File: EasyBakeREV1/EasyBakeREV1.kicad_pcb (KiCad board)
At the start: 2 copper layers, 100 x 71.2 mm, 105 parts, among them J1 I2C OUT, U1 MIC5219-3.3YM5, U2 USBLC6-2SC6, U3 PCA9702, U4 SQ2310ES_SOT23, U5 NHD-C12832A1Z, U6 SQ2310ES_SOT23, U7 MAX31855_SO8, U8 LM324, U9 SN74LVC1G32, Y1 16MHz

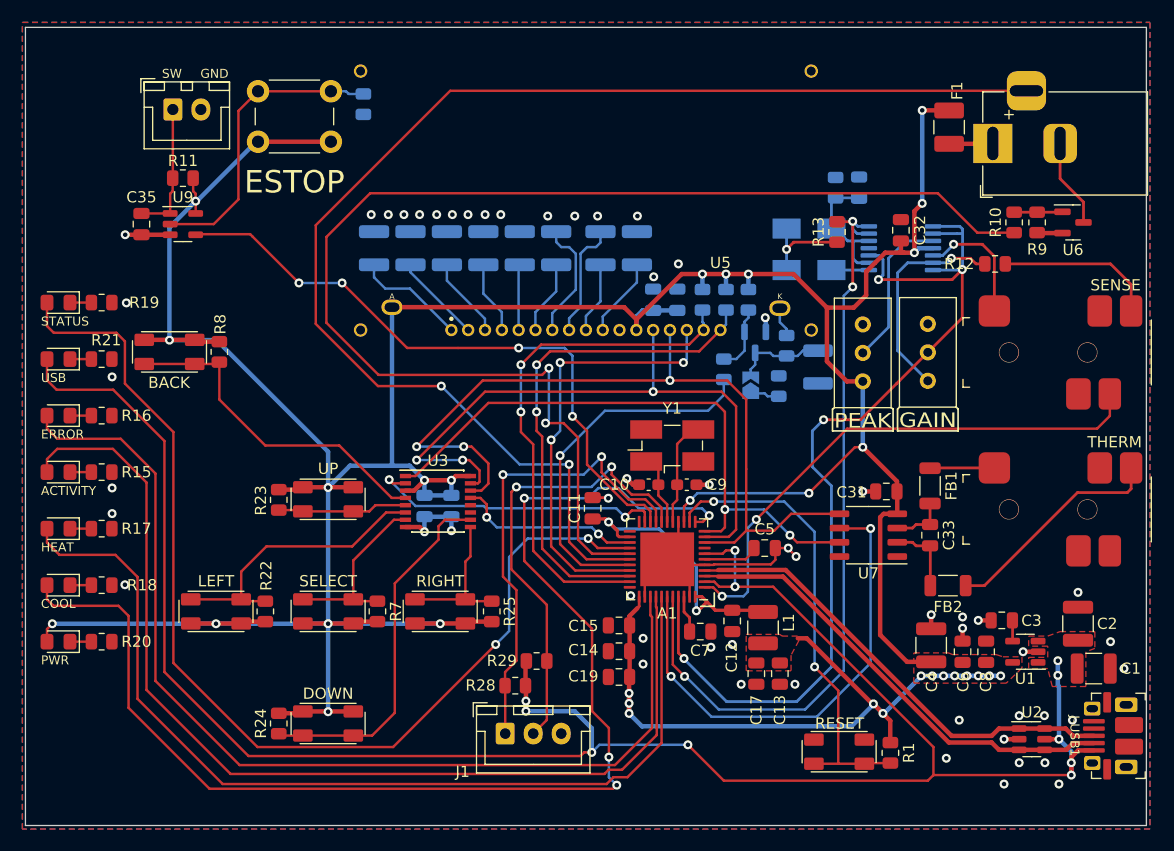
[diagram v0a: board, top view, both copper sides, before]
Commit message: REV3 - Reorganize MC pinouts and add LED driver (WIP)
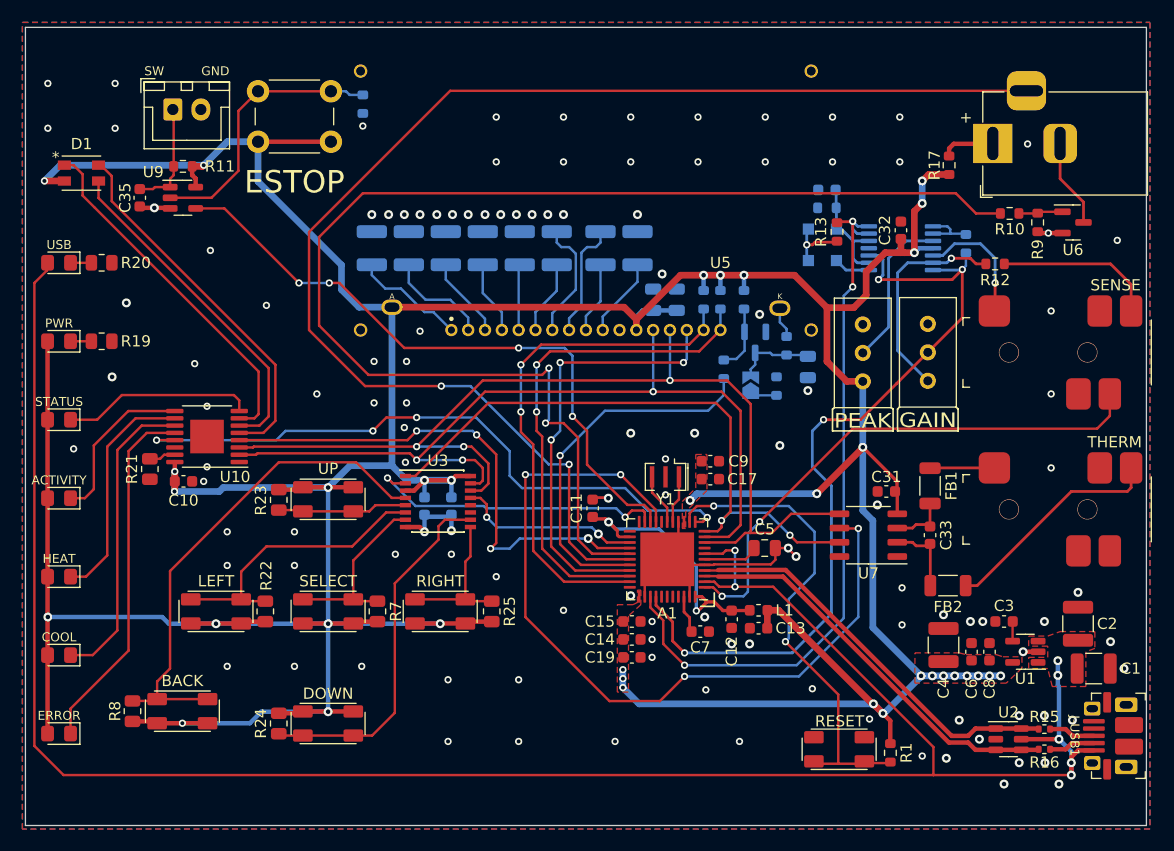
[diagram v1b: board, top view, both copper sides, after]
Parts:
- removed F1: Polyfuse_Small, Fuse:Fuse_1210_3225Metric_Pad1.42x2.65mm_HandSolder
- removed J1: I2C OUT, Connector_JST:JST_XH_B3B-XH-A_1x03_P2.50mm_Vertical
- removed R28, R29: 4.7K, Resistor_SMD:R_0805_2012Metric
- added D1: LED_RGBA, Daxxn_LEDs:IN-P32TATRGB, F.Cu at (20.0, 33.0)
- added U10: STP08CP05, Package_SO:TSSOP-16-1EP_4.4x5mm_P0.65mm_EP3x3mm, F.Cu at (31.2, 56.5)
- C10, C9: value 22pF -> 100nF; footprint Capacitor_SMD:C_0603_1608Metric_Pad1.08x0.95mm_HandSolder -> Capacitor_SMD:C_0603_1608Metric
- C11, C12, C13, C14, C15, C16, C17, C18, C19, C3, C33, C35, C6, C7, C8: footprint Capacitor_SMD:C_0805_2012Metric -> Capacitor_SMD:C_0603_1608Metric
- C25: footprint Resistor_SMD:R_1210_3225Metric -> Capacitor_SMD:C_0805_2012Metric
- C31, C32, C34: value ${DCPL-CAP} -> 100nF; footprint Capacitor_SMD:C_0805_2012Metric -> Capacitor_SMD:C_0603_1608Metric
- D5, D6: footprint Diode_SMD:D_SMA -> Diode_SMD:D_SOD-323_HandSoldering
- L1: value 1uH -> 100nH; footprint Inductor_SMD:L_1210_3225Metric -> Inductor_SMD:L_0603_1608Metric
- R1, R10, R11, R12, R2, R26, R27, R3, R4, R5, R6: footprint Resistor_SMD:R_0805_2012Metric -> Resistor_SMD:R_0603_1608Metric
- R13, R14, R9: value ${PULLUP-RES} -> 10K; footprint Resistor_SMD:R_0805_2012Metric -> Resistor_SMD:R_0603_1608Metric
- R15, R16: value 220 -> 22; footprint Resistor_SMD:R_0805_2012Metric -> Resistor_SMD:R_0402_1005Metric
- R17: value 220 -> 100; footprint Resistor_SMD:R_0805_2012Metric -> Resistor_SMD:R_0603_1608Metric
- R18: value 220 -> 100; footprint Resistor_SMD:R_0805_2012Metric -> Resistor_SMD:R_0603_1608Metric; moved to B.Cu
- R19, R20: value 220 -> 1K
- R21: value 220 -> 2K
- R22, R23, R24, R25, R7, R8: value ${PULLUP-RES} -> 10K
- Y1: value 16MHz -> 12MHz; footprint Crystal:Crystal_SMD_EuroQuartz_MJ-4Pin_5.0x3.2mm_HandSoldering -> Crystal:Resonator_SMD_Murata_CSTxExxV-3Pin_3.0x1.1mm
- moved R16 89.2 mm to (105.9, 84.4), turned to 180 degrees
- moved R15 87.2 mm to (105.9, 82.6), turned to 180 degrees
- moved R18 82.9 mm to (98.9, 39.3), turned to 90 degrees
- moved R17 82.3 mm to (97.4, 32.3), turned to -90 degrees
- moved C10 41.5 mm to (29.1, 60.5)
- moved R20 33.8 mm to (21.8, 41.0)
- moved R8 33.0 mm to (24.6, 81.0), turned to -90 degrees
- moved SW-M-BK1 32.1 mm to (29.0, 81.0), turned to 0 degrees
- moved D-ERR1 28.4 mm to (18.0, 83.0)
- moved D-PWR1 26.8 mm to (18.0, 48.0)
- moved C17 17.8 mm to (76.1, 60.3), turned to 0 degrees
- moved R21 10.7 mm to (26.1, 59.4), turned to -90 degrees
- moved D-STA1 10.5 mm to (18.0, 55.0)
- moved D-USB1 8.59 mm to (18.0, 41.0)
- moved D-COOL1 6.24 mm to (18.0, 76.0)
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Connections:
- A1 pad 12: /LED-COOL -> /IND-OE
- A1 pad 18: I2C-SCLK -> unconnected-(A1-Pad18)
- A1 pad 19: I2S-SDA -> /THERM-CS
- A1 pad 26: /LED-STA -> /IND-LE
- A1 pad 36: /LED-ERR -> /CURR-PEAK
- A1 pad 37: /LED-ACT -> /CURR-SENSE
- A1 pad 38: /LED-HEAT -> unconnected-(A1-Pad38)
- A1 pad 39: /THERM-CS -> unconnected-(A1-Pad39)
- A1 pad 40: /CURR-PEAK -> unconnected-(A1-Pad40)
- A1 pad 41: /CURR-SENSE -> unconnected-(A1-Pad41)
- C10 pad 1: GND -> VCC
- C10 pad 2: Net-(A1-Pad17) -> GND
- C9 pad 1: GND -> VCC
- C9 pad 2: Net-(A1-Pad16) -> GND
- D-ACT1 pad 1: Net-(D-ACT1-Pad1) -> /Indicators/IND-ACT
- D-ACT1 pad 2: /LED-ACT -> VCC
- D-COOL1 pad 1: Net-(D-COOL1-Pad1) -> /Indicators/IND-COOL
- D-COOL1 pad 2: /LED-COOL -> VCC
- D-ERR1 pad 1: Net-(D-ERR1-Pad1) -> /Indicators/IND-ERR
- D-ERR1 pad 2: /LED-ERR -> VCC
- D-HEAT1 pad 1: Net-(D-HEAT1-Pad1) -> /Indicators/IND-HEAT
- D-HEAT1 pad 2: /LED-HEAT -> VCC
- D-STA1 pad 1: Net-(D-STA1-Pad1) -> /Indicators/IND-STATUS
- D-STA1 pad 2: /LED-STA -> VCC
- J-HTR1 pad 1: Net-(F1-Pad2) -> Net-(J-HTR1-Pad1)
- J-USB1 pad 2: /USBIN- -> Net-(J-USB1-Pad2)
- J-USB1 pad 3: /USBIN+ -> Net-(J-USB1-Pad3)
- R15 pad 1: Net-(D-ACT1-Pad1) -> Net-(J-USB1-Pad3)
- R15 pad 2: GND -> /USBIN+
- R16 pad 1: Net-(D-ERR1-Pad1) -> Net-(J-USB1-Pad2)
- R16 pad 2: GND -> /USBIN-
- R17 pad 1: Net-(D-HEAT1-Pad1) -> Net-(J-HTR1-Pad1)
- R17 pad 2: GND -> VCC
- R18 pad 1: Net-(D-COOL1-Pad1) -> /CURR-SENSE
- R18 pad 2: GND -> Net-(U8-Pad1)
- R19 pad 1: Net-(D-STA1-Pad1) -> Net-(D-PWR1-Pad1)
- R20 pad 1: Net-(D-PWR1-Pad1) -> Net-(D-USB1-Pad1)
- R21 pad 1: Net-(D-USB1-Pad1) -> Net-(U10-Pad15)
- U8 pad 1: /CURR-SENSE -> Net-(U8-Pad1)
- U8 pad 2: /CURR-SENSE -> Net-(U8-Pad1)
- Y1 pad 1: Net-(A1-Pad17) -> Net-(A1-Pad16)
- Y1 pad 2: unconnected-(Y1-Pad2) -> GND
- Y1 pad 3: Net-(A1-Pad16) -> Net-(A1-Pad17)
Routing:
- net /LED-COOL: track 112.4 -> 0.00 mm, vias 4 -> 0
- net /LED-STA: track 95.8 -> 0.00 mm, vias 2 -> 0
- net /LED-ACT: track 92.6 -> 0.00 mm
- net /LED-ERR: track 91.5 -> 0.00 mm
- net /LED-HEAT: track 85.9 -> 0.00 mm
- net /IND-OE: track 0.00 -> 57.8 mm, vias 0 -> 4
- net VCC: track 387.8 -> 444.9 mm, vias 32 -> 35
- net /IND-LE: track 0.00 -> 45.9 mm, vias 0 -> 4
- net I2S-SDA: track 42.2 -> 0.00 mm, vias 2 -> 0
- net I2C-SCLK: track 40.9 -> 0.00 mm, vias 2 -> 0
- net /Indicators/IND-BLUE: track 0.00 -> 33.1 mm
- net /Indicators/IND-ERR: track 0.00 -> 32.1 mm
- net /Indicators/IND-RED: track 0.00 -> 31.7 mm
- net /Indicators/IND-GREEN: track 0.00 -> 30.2 mm
- net /THERM-CS: track 43.3 -> 72.2 mm, vias 2 -> 4
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
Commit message: Update to KiCad 7
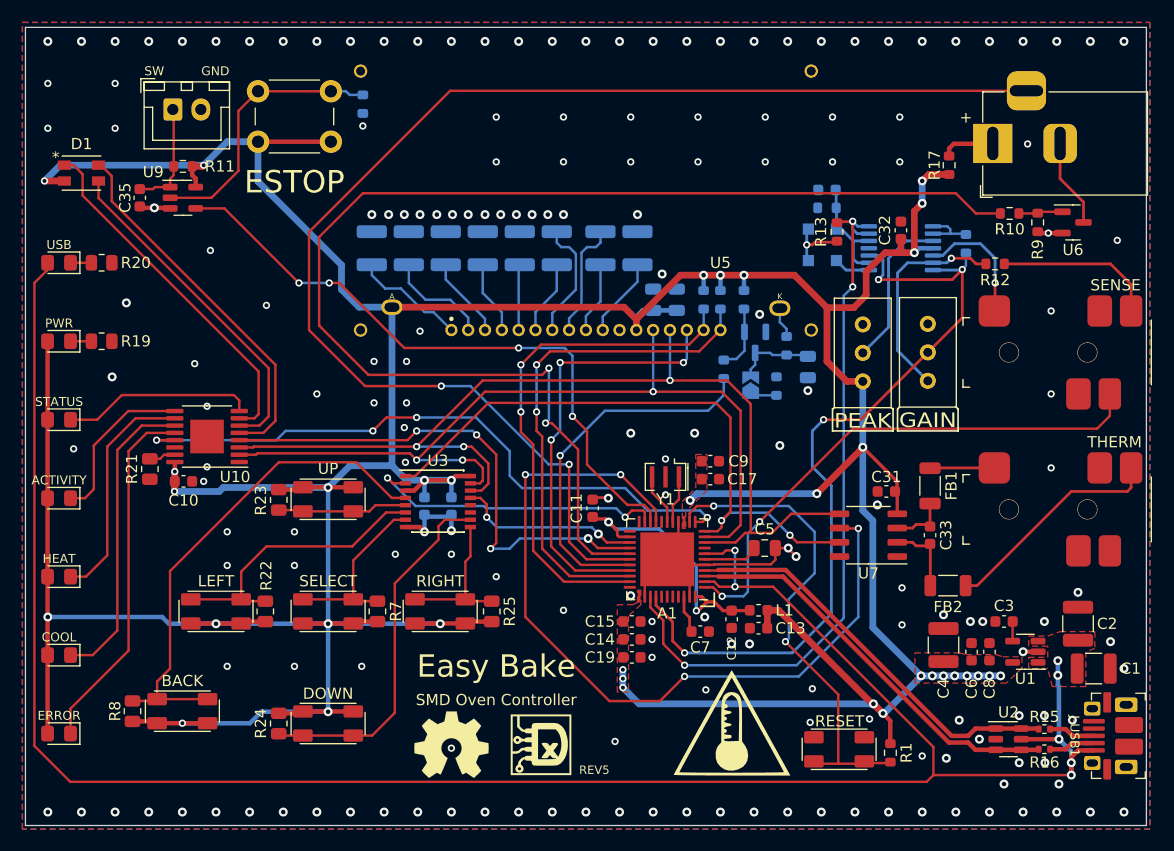
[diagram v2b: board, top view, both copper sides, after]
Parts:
- added G***: LOGO, Daxxn_Logos_Art:Thermometer_N, F.Cu at (78.0, 82.0)
- added G***: LOGO, Daxxn_Logos_Art:Daxxn_Logo_S, F.Cu at (61.0, 84.0)
- added REF**: OSHW-Symbol_6.7x6mm_SilkScreen, Symbol:OSHW-Symbol_6.7x6mm_SilkScreen, F.Cu at (53.0, 84.0)
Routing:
- net /HTR-PWM: track 116.3 -> 115.7 mm
- net GND: vias 119 -> 184
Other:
- board text added: "Easy Bake"
- board text added: "REV5"
- board text added: "SMD Oven Controller"

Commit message: Change main pwr to 3.3 due to USB issues
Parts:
- removed D-PWR1: YELLOW, LED_SMD:LED_0805_2012Metric_Pad1.15x1.40mm_HandSolder
- removed JP-PWM-BYP1: SolderJumper_2_Open, Jumper:SolderJumper-2_P1.3mm_Open_TrianglePad1.0x1.5mm
- removed R26: 10K, Resistor_SMD:R_0603_1608Metric
- removed REF**: OSHW-Symbol_6.7x6mm_SilkScreen, Symbol:OSHW-Symbol_6.7x6mm_SilkScreen
- added C36: 10uF, Capacitor_SMD:C_1210_3225Metric, F.Cu at (-28.3, 52.8)
- added C37: 1uF, Capacitor_SMD:C_1210_3225Metric, B.Cu at (81.8, 83.7)
- added C38: 10uF, Capacitor_SMD:C_1210_3225Metric, F.Cu at (-28.3, 61.3)
- added C39: 100nF, Capacitor_SMD:C_0603_1608Metric, F.Cu at (-23.4, 51.9)
- added C40: 100nF, Capacitor_SMD:C_0603_1608Metric, F.Cu at (-23.4, 54.4)
- added C41: 470pF, Capacitor_SMD:C_0603_1608Metric, F.Cu at (-23.4, 56.9)
- added C42: 100nF, Capacitor_SMD:C_0805_2012Metric, F.Cu at (-19.2, 52.2)
- added C43: 100nF, Capacitor_SMD:C_0805_2012Metric, F.Cu at (-19.2, 55.2)
- added D-TX1: YELLOW, LED_SMD:LED_0805_2012Metric_Pad1.15x1.40mm_HandSolder, F.Cu at (4.00, 39.0)
- added D-VCC1: YELLOW, LED_SMD:LED_0805_2012Metric_Pad1.15x1.40mm_HandSolder, F.Cu at (18.0, 48.0)
- added D-VDD2: YELLOW, LED_SMD:LED_0805_2012Metric_Pad1.15x1.40mm_HandSolder, F.Cu at (-17.8, 73.0)
- added Q1: MMBT2222A, Package_TO_SOT_SMD:SOT-23, F.Cu at (-35.5, 48.0)
- added Q2: MMBT2222A, Package_TO_SOT_SMD:SOT-23, F.Cu at (-35.5, 57.3)
- added Q3: MMBT2222A, Package_TO_SOT_SMD:SOT-23, F.Cu at (-35.5, 61.8)
- added Q4: MMBT2222A, Package_TO_SOT_SMD:SOT-23, F.Cu at (-20.8, 66.8)
- added R28: 330, Resistor_SMD:R_0603_1608Metric, F.Cu at (8.00, 39.0)
- added R29: 10K, Resistor_SMD:R_0603_1608Metric, F.Cu at (-32.0, 47.0)
- added R30: 10K, Resistor_SMD:R_0603_1608Metric, F.Cu at (-32.0, 56.0)
- added R31: 10K, Resistor_SMD:R_0603_1608Metric, F.Cu at (-40.0, 56.9)
- added R32: 1K, Resistor_SMD:R_0603_1608Metric, F.Cu at (-40.0, 59.5)
- added R33: 1K, Resistor_SMD:R_0603_1608Metric, F.Cu at (-40.0, 62.0)
- added R34: 1K, Resistor_SMD:R_0603_1608Metric, F.Cu at (-40.0, 64.5)
- added R35: 10K, Resistor_SMD:R_0603_1608Metric, F.Cu at (-40.0, 67.0)
- added R36: 10K, Resistor_SMD:R_0603_1608Metric, F.Cu at (-40.0, 69.5)
- added R37: 10K, Resistor_SMD:R_0603_1608Metric, F.Cu at (-40.0, 72.0)
- added R38: 10K, Resistor_SMD:R_0603_1608Metric, F.Cu at (-29.1, 66.7)
- added R39: 1K, Resistor_SMD:R_0603_1608Metric, F.Cu at (-29.1, 69.2)
- added R40: 10K, Resistor_SMD:R_0603_1608Metric, F.Cu at (-29.1, 71.7)
- added R41: 100, Resistor_SMD:R_0603_1608Metric, F.Cu at (-29.1, 74.2)
- added R42: 100, Resistor_SMD:R_0603_1608Metric, F.Cu at (-29.1, 76.7)
- added R43: 330, Resistor_SMD:R_0805_2012Metric, F.Cu at (-13.2, 66.9)
- added U11: MIC5219-5.0YM5, Package_TO_SOT_SMD:SOT-23-5, F.Cu at (104.2, 75.7)
- added U12: NLSV2T244MU, Package_DFN_QFN:OnSemi_UDFN-8_1.2x1.8mm_P0.4mm, F.Cu at (80.0, 58.0)
- moved U1 64.0 mm to (47.1, 104.6)
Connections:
- A1 pad 10: SPI-COPI -> /SPI-COPI-ARD
- A1 pad 8: unconnected-(A1-Pad8) -> /TX-IND
- A1 pad 9: SPI-SCLK -> /SPI-SCLK-ARD
- C27 pad 1: VCC -> VDD
- C28 pad 1: VCC -> VDD
- C31 pad 1: VCC -> VDD
- C4 pad 1: VCC -> VDD
- C6 pad 1: VCC -> VDD
- C8 pad 1: VCC -> VDD
- J-SENSE1 pad SW: /CURR-SENSE-SW -> Net-(J-SENSE1-PadSW)
- R1 pad 1: VCC -> unconnected-(R1-Pad1)
- R2 pad 1: VCC -> VDD
- R2 pad 2: /DISP-RESET -> /Display/DISP-~{RESET}-B
- R3 pad 1: VCC -> VDD
- R3 pad 2: /DISP-CS -> /Display/DISP-~{CS}-B
- U1 pad 5: VCC -> VDD
- U3 pad 3: VCC -> VDD
- U5 pad 12: VCC -> VDD
- U5 pad 15: /DISP-A0 -> /Display/DISP-A0-B
- U5 pad 16: /DISP-RESET -> /Display/DISP-~{RESET}-B
- U5 pad 17: /DISP-CS -> /Display/DISP-~{CS}-B
- U5 pad A: VCC -> VDD
- U7 pad 4: VCC -> VDD
- U7 pad 6: /THERM-CS -> /Sensing/THERM-~{CS}-B
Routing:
- net SPI-COPI: track 76.1 -> 62.3 mm
- net SPI-SCLK: track 88.7 -> 77.2 mm
- net VCC: track 444.9 -> 437.7 mm
- net /SPI-COPI-ARD: track 0.00 -> 3.65 mm
- net Net-(JP-PWM-BYP1-Pad1): track 2.37 -> 0.00 mm
- net (no net): track 0.00 -> 2.37 mm
- net GND: vias 184 -> 183
